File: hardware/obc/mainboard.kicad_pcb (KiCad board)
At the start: 6 copper layers, 95.9 x 90.2 mm, 216 parts, among them J101 Conn_02x20_Odd_Even, J301 USB_C_Receptacle_USB2.0, J302 Conn_High-Rel_4S2P_Vertical, J303 Conn_01x06, J304 Conn_High-Rel_6P, J305 Conn_01x05, J601 Conn_01x08_Socket, J602 SMA RA Connector, J603 SMA RA Connector, J604 SMA RA Connector, Q201 BSS138DWQ-7, Q202 BSS138DWQ-7, Q203 MBT2222ADW1T1, Q204 MBT2222ADW1T1, Q205 BSS138DWQ-7, Q206 BSS138DWQ-7, Q207 MBT2222ADW1T1, Q208 MBT2222ADW1T1, Q209 MMDT2907, Q401 MBT2222ADW1T1, Q402 MBT2222ADW1T1, Q403 IRLML2803, Q404 IRF7406PbF, Q501 MMBT2222AT, Q502 IRLML2803, Q503 IRLML2803, Q504 IRLML2803, Q505 IRF7406PbF, Q506 IRF7406PbF, Q507 IRF7406PbF, U101 MAX706RESA, U102 ATSAMD51J20A-AU, U103 BMI088, U301 Mem_MT29F4G01ABAFDWB, U302 Mem_MT29F4G01ABAFDWB, U401 TPS7A4501DCQT, U402 LTC4121, U403 TPS54226PWPRPWP14_2P31X2P46-L, U404 ADM1176-1ARMZ-R7, U405 BQ25886RGER, U501 PE014006, U601 RFM98PW, U602 S1216V8, U603 GP2S1+, Y101 32.768kHz

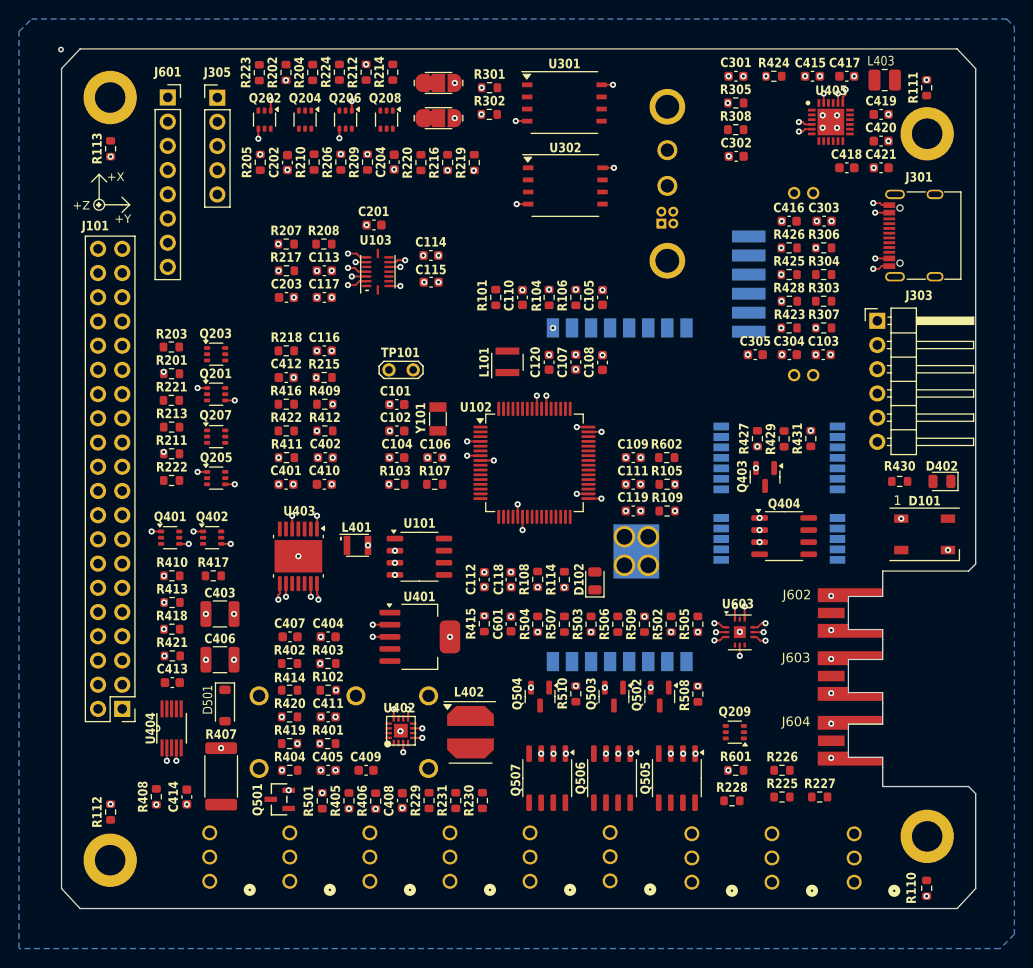
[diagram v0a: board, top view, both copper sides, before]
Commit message: obc: test traces for high priority signals
Preliminary trace creation for high priority signals.
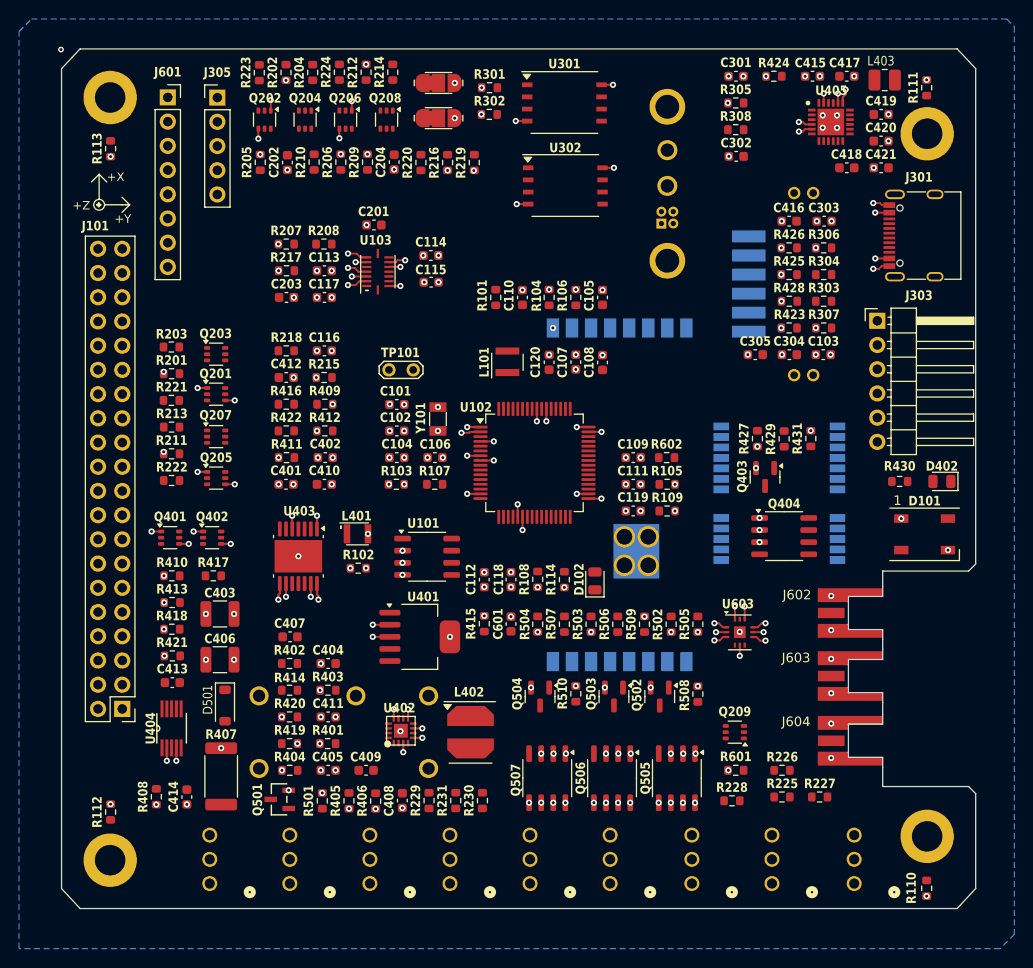
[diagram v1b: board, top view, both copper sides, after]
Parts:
- moved JP507 17.0 mm to (184.0, 145.8)
- moved JP509 17.0 mm to (167.0, 145.8)
- moved R102 13.2 mm to (132.0, 112.7), turned to 0 degrees
- moved C404 2.80 mm to (128.8, 122.7)
- moved R403 2.80 mm to (128.8, 125.5)
- moved L401 1.20 mm to (131.8, 109.1)
- moved U101 0.80 mm to (139.2, 111.5)
- moved JP503 0.28 mm to (158.4, 145.8)
- moved JP501 0.24 mm to (116.4, 145.8)
- moved JP502 0.24 mm to (133.2, 145.8)
- moved JP504 0.24 mm to (124.8, 145.8)
- moved JP505 0.24 mm to (150.0, 145.8)
- moved JP506 0.24 mm to (141.6, 145.8)
- moved JP508 0.15 mm to (175.4, 145.8)
- moved R103 0.05 mm to (136.0, 103.9)
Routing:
- net /Burn Wires/VBURN1: track 0.00 -> 23.8 mm, vias 0 -> 4
- net /Avionics/BATTERY: track 0.00 -> 23.2 mm, vias 0 -> 4
- net /Burn Wires/VBURN2: track 0.00 -> 21.4 mm, vias 0 -> 4
- net /Burn Wires/VBURN3: track 0.00 -> 19.1 mm, vias 0 -> 4
- net /Avionics/XTAL1: track 0.00 -> 10.0 mm, vias 0 -> 3
- net /Avionics/XTAL2: track 0.00 -> 8.86 mm, vias 0 -> 3

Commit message: obc: more test routing
Getting a feel for the problem space regarding traces by way of test routing.
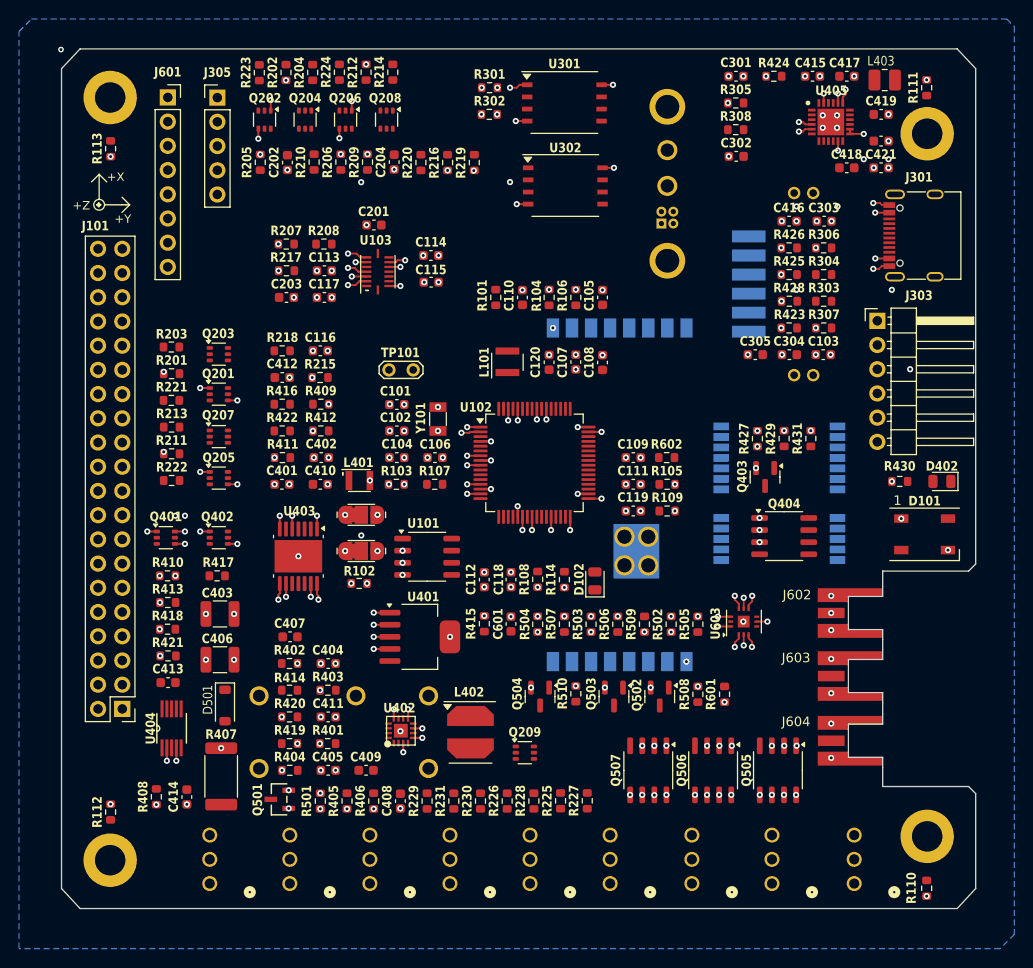
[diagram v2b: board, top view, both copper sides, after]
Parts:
- moved JP402 46.1 mm to (132.3, 110.9)
- moved JP401 46.0 mm to (132.3, 107.1)
- moved R226 29.0 mm to (147.6, 137.1), turned to 90 degrees
- moved R227 24.4 mm to (156.0, 137.1), turned to -90 degrees
- moved R225 23.2 mm to (153.2, 137.1), turned to 90 degrees
- moved Q209 22.1 mm to (149.4, 132.1), turned to 0 degrees
- moved R228 20.8 mm to (150.4, 137.1), turned to 90 degrees
- moved Q505 10.6 mm to (176.0, 133.9)
- moved Q506 10.6 mm to (169.2, 133.9)
- moved Q507 10.6 mm to (162.4, 133.9)
- moved R601 8.06 mm to (170.4, 125.9), turned to 90 degrees
- moved L401 5.60 mm to (132.0, 103.5)
- moved R102 1.60 mm to (132.1, 114.3)
- moved U603 1.18 mm to (172.4, 118.3), turned to 90 degrees
- moved Q402 0.70 mm to (117.3, 109.5)
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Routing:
- net FLASH_CS1: track 0.00 -> 85.4 mm, vias 0 -> 6
- net BURN_RELAY_A: track 0.00 -> 61.8 mm, vias 0 -> 3
- net AIN5: track 0.00 -> 50.2 mm, vias 0 -> 1
- net /Power/REGN: track 0.00 -> 50.0 mm, vias 0 -> 7
- net ENAB_BURN1: track 0.00 -> 37.2 mm, vias 0 -> 3
- net BAT_1&2: track 0.00 -> 34.8 mm, vias 0 -> 5
- net ENAB_GPS: track 0.00 -> 32.5 mm, vias 0 -> 3
- net ENAB_RF: track 0.00 -> 27.3 mm, vias 0 -> 2
- net ENAB_BURN3: track 0.00 -> 27.2 mm, vias 0 -> 3
- net /Power/V_RF: track 0.00 -> 25.2 mm, vias 0 -> 5
- net /Burn Wires/VBURN1: track 23.8 -> 0.00 mm
- net /Power/3V3_EN: track 0.00 -> 21.4 mm, vias 0 -> 5
- net /Burn Wires/VBURN2: track 21.4 -> 0.00 mm
- net /RF and GPS/RF1_ANT: track 0.00 -> 19.8 mm, vias 0 -> 2
- net /Burn Wires/VBURN3: track 19.1 -> 0.00 mm
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- added copper zone on In3.Cu, net /Burn Wires/VBURN1
- added copper zone on In3.Cu, net /Burn Wires/VBURN2
- added copper zone on In3.Cu, net /Burn Wires/VBURN3

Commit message: obc: more preliminary routing
Still exploring problem space regarding routing, ~100 routed nets added.
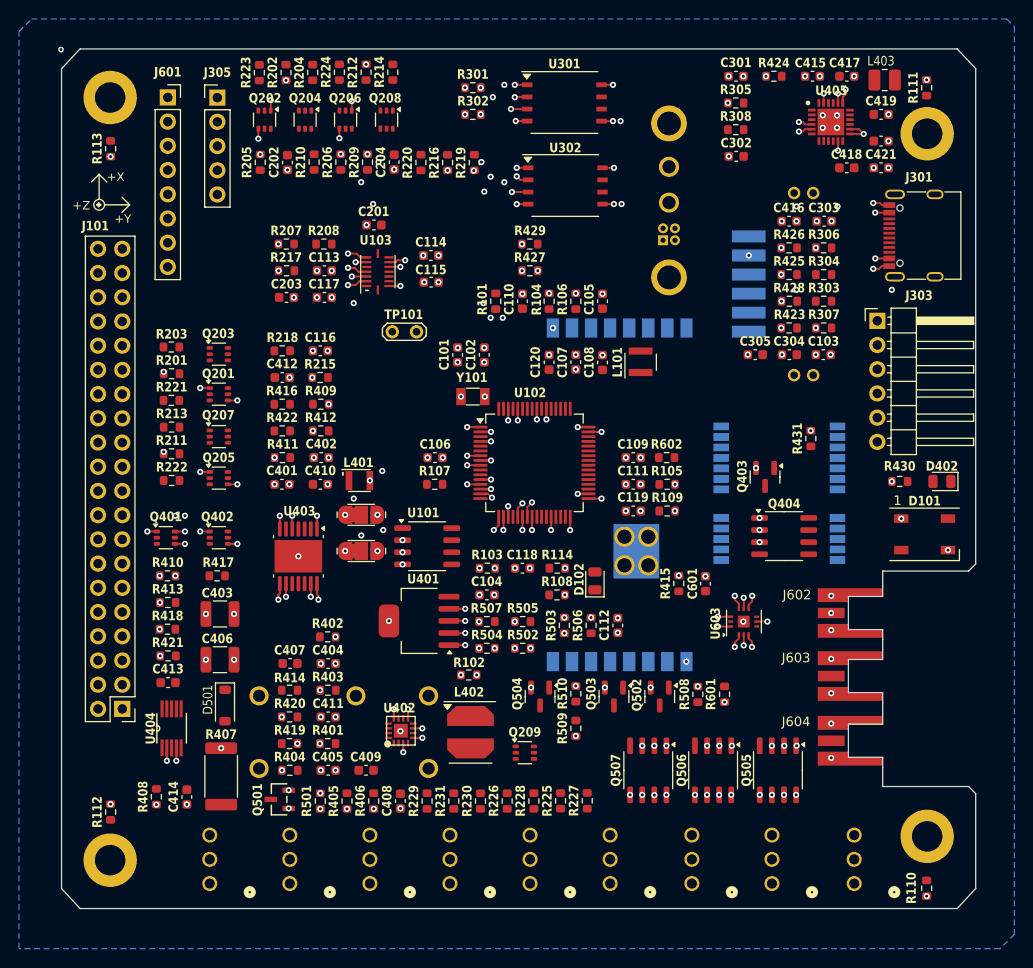
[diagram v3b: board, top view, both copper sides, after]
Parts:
- moved R429 33.6 mm to (150.0, 78.7), turned to 0 degrees
- moved R427 29.7 mm to (150.0, 81.5), turned to 0 degrees
- moved C601 20.8 mm to (168.4, 114.3)
- moved R415 20.8 mm to (165.6, 114.3)
- moved R505 18.4 mm to (149.2, 118.3), turned to 180 degrees
- moved C104 17.2 mm to (145.5, 115.5), turned to 0 degrees
- moved R502 15.8 mm to (149.2, 121.1), turned to 0 degrees
- moved R102 15.0 mm to (143.6, 123.9)
- moved C112 14.8 mm to (159.2, 118.7)
- moved L101 14.0 mm to (161.6, 91.1)
- moved R509 13.1 mm to (154.8, 129.5)
- moved R103 13.0 mm to (145.5, 112.7), turned to 180 degrees
- moved C102 12.2 mm to (145.2, 90.3), turned to 90 degrees
- moved C101 8.23 mm to (142.4, 90.3), turned to 90 degrees
- moved R507 8.13 mm to (145.5, 118.3), turned to 180 degrees
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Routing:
- net FLASH_MOSI: track 0.00 -> 86.3 mm, vias 0 -> 7
- net FLASH_IO2: track 0.00 -> 78.6 mm, vias 0 -> 7
- net FLASH_CS2: track 0.00 -> 66.4 mm, vias 1 -> 6
- net FLASH_MISO: track 0.00 -> 55.9 mm, vias 0 -> 7
- net ENAB_GPS: track 32.5 -> 20.5 mm
- net ENAB_BURN1: track 37.2 -> 25.7 mm
- net /Power/V_RF: track 25.2 -> 32.4 mm
- net ENAB_RF: track 27.3 -> 20.4 mm
- net ENAB_BURN3: track 27.2 -> 21.1 mm
- net /Burn Wires/VBURN_A_IN: track 13.0 -> 17.5 mm
- net BAT_1&2: track 34.8 -> 30.4 mm, vias 5 -> 2
- net /Avionics/BATTERY: track 24.8 -> 21.1 mm
- net /RF and GPS/RF1_ANT: track 19.8 -> 17.3 mm
- net AIN5: track 50.2 -> 48.1 mm
- net BURN_RELAY_A: track 61.8 -> 59.7 mm
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
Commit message: Adjust zone fills for burnwire
Attempt to lower resistance.
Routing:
- added copper zone on In4.Cu, net /Burn Wires/VBURN1
- added copper zone on In4.Cu, net /Burn Wires/VBURN2
- added copper zone on In4.Cu, net /Burn Wires/VBURN3
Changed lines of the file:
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@@
 		(polygon
 			(pts
-				(xy 196.799928 57.5) (xy 173.599928 57.5) (xy 173.599928 75.9) (xy 160.8 75.9) (xy 160.8 80.028418)
-				(xy 173.361696 93.1) (xy 184.799928 93.1) (xy 184.799928 101.1) (xy 196.799928 101.1)
+				(xy 196.8 57.5) (xy 173.6 57.5) (xy 173.6 73.5) (xy 160.4 73.5) (xy 160.4 78.444206) (xy 175.397834 93.521306)
+				(xy 177.510719 93.528083) (xy 184.8 101.1) (xy 196.8 101.1)
 			)
 		)
@@
 		(net 82)
 		(net_name "/Burn Wires/VBURN2")
-		(layer "In3.Cu")
+		(layers "In3.Cu" "In4.Cu")
 		(hatch edge 0.5)
 		(priority 8)
@@
 		(polygon
 			(pts
-				(xy 178.2 137.7) (xy 173 137.7) (xy 173 135.5) (xy 166.6 135.5) (xy 166.6 138.130078) (xy 171.2 138.155694)
-				(xy 171.2 141.9) (xy 178.2 141.9)
+				(xy 177.2 138.8) (xy 173.3 137.8) (xy 173 135.5) (xy 166.6 135.5) (xy 166.6 138.8) (xy 169 141.9)
+				(xy 171.2 141.9) (xy 177.2 141.9)
 			)
 		)
@@
 		(net 81)
 		(net_name "/Burn Wires/VBURN1")
-		(layer "In3.Cu")
+		(layers "In3.Cu" "In4.Cu")
 		(hatch edge 0.5)
 		(priority 7)
@@
 		(polygon
 			(pts
-				(xy 185.4 135.5) (xy 173.4 135.5) (xy 173.4 137.3) (xy 178.6 137.3) (xy 178.6 141.9) (xy 185.4 141.9)
+				(xy 186.7 138.8) (xy 179.9 135.5) (xy 173.4 135.5) (xy 173.4 138.8) (xy 176.8 138.8) (xy 176.8 141.9)
+				(xy 186.7 141.9)
 			)
 		)
@@
 		(net 83)
 		(net_name "/Burn Wires/VBURN3")
-		(layer "In3.Cu")
+		(layers "In3.Cu" "In4.Cu")
 		(hatch edge 0.5)
 		(priority 9)
@@
 		(polygon
 			(pts
-				(xy 170.8 141.9) (xy 170.8 138.528964) (xy 166.2 138.528964) (xy 166.2 135.5) (xy 160 135.5) (xy 160 141.9)
+				(xy 169 141.9) (xy 169 138.8) (xy 166.3 137.8) (xy 166.2 135.5) (xy 160 135.5) (xy 160 138.7) (xy 162.5 141.9)
 			)
 		)

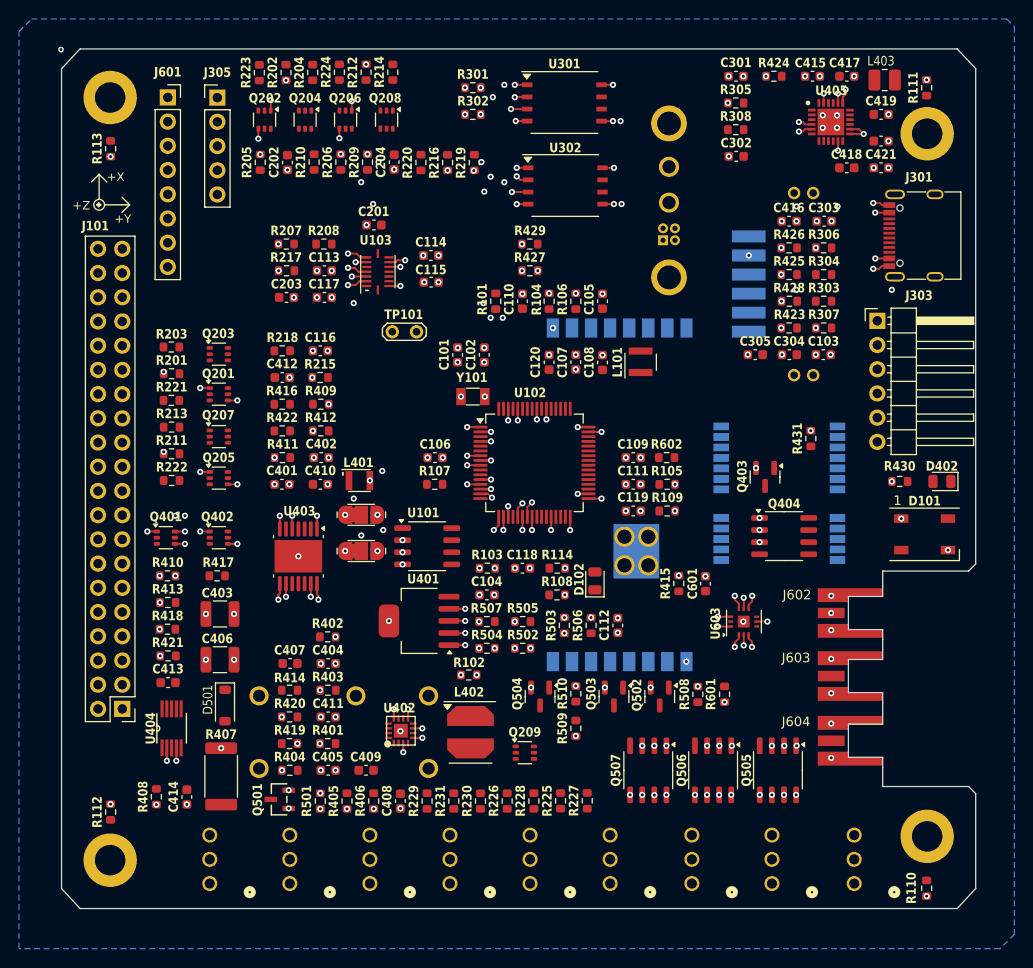
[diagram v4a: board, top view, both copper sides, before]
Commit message: obc: more routing
Added new and edited existing traces.
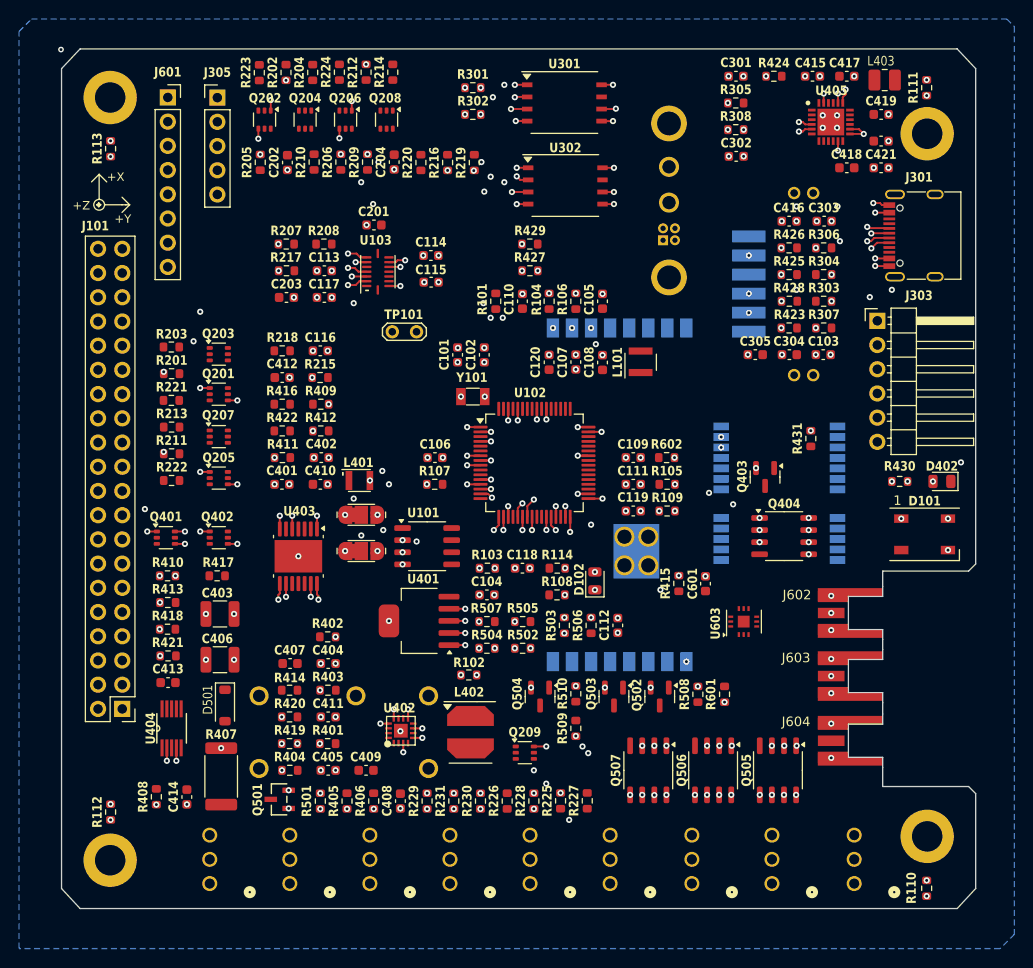
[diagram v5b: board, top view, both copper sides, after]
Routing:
- net MISO_RF1: track 0.00 -> 128.9 mm, vias 0 -> 6
- net MOSI_RF1: track 0.00 -> 109.4 mm, vias 0 -> 5
- net MISO: track 0.00 -> 107.2 mm, vias 0 -> 8
- net MOSI: track 0.00 -> 84.8 mm, vias 0 -> 3
- net FLASH_SCK: track 1.71 -> 84.9 mm, vias 1 -> 5
- net Net-(D101-DIN): track 0.00 -> 49.5 mm, vias 0 -> 3
- net L1_PROG: track 0.00 -> 41.5 mm, vias 0 -> 4
- net AIN5: track 48.1 -> 77.8 mm
- net GPS_PWR_IN: track 0.00 -> 25.8 mm, vias 0 -> 8
- net Net-(D102-K): track 0.00 -> 15.2 mm, vias 0 -> 3
- net Net-(J301-D--PadA7): track 0.00 -> 15.1 mm, vias 0 -> 4
- net Net-(J301-D+-PadA6): track 0.00 -> 13.2 mm, vias 0 -> 4
- net GND: track 52.2 -> 40.2 mm, vias 114 -> 104
- net Net-(D102-A): track 0.00 -> 11.4 mm, vias 0 -> 3
- net Net-(H101-Pad1): track 0.00 -> 4.64 mm, vias 0 -> 1
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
